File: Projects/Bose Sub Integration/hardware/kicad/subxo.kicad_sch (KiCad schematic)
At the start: 39 parts, among them J1 IN L, J2 IN R, J3 OUT 3.5mm, J4 PWR IN 15V, J5 POLARITY SW, J6 LEVEL POT 10k, U1 TL074, U2 LM7812

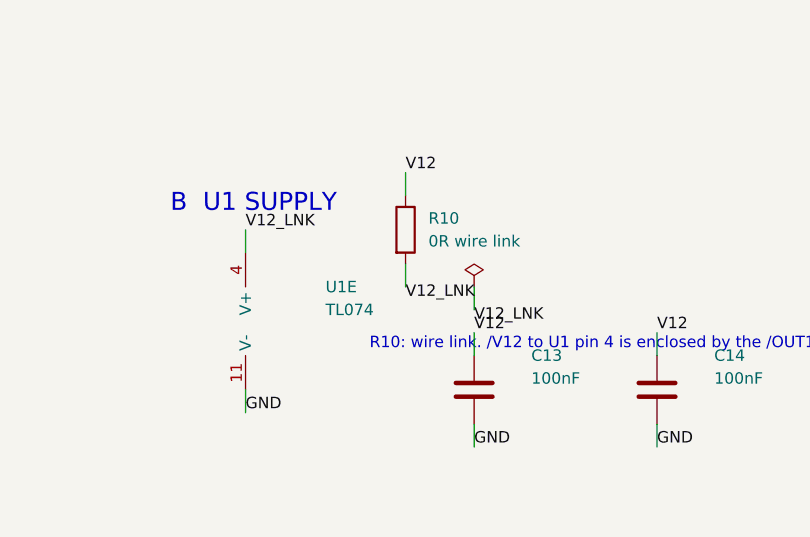
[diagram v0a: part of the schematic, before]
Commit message: Sub crossover board: re-placed, and the wire link is gone
The board committed in 28a28b6 only closed single-sided with R10, a 0 ohm
link flying over the tracks that sealed off U1 pin 4. Re-placing the parts
dissolves that pocket: /V12 now reaches pin 4 in copper. R10, the /V12_LNK
net it needed and the PWR_FLAG that marked that net as driven are all gone
from both the schematic and the layout.

185 track segments, every one on B.Cu, no vias and no top copper. DRC
reports 0 unconnected pads. The 15 violations that remain are silkscreen
only -- 12 overlaps and 3 clipped by mask -- and silkscreen is not in the
etched artwork, so none of them reach the board.

Outline comes down from 120.05 x 100.05 mm to 96.90 x 100.20 mm.

Zone rules now match the process instead of the KiCad defaults: minimum
clearance 0.5 -> 0.85 mm, and pads connect solid rather than through
thermal spokes.

Production files re-exported for the single-sided flow: B.Cu and Edge_Cuts
only, plus PTH drills, 100 holes across 0.8 / 1.0 / 1.1 / 1.2 / 1.52 mm.
The old two-sided set is dropped -- F.Cu, both solder masks, silkscreen and
the fab layer were never going to be made. The NPTH file exports empty.
Schematic is migrated to the KiCad 10 file format and stamped rev A.
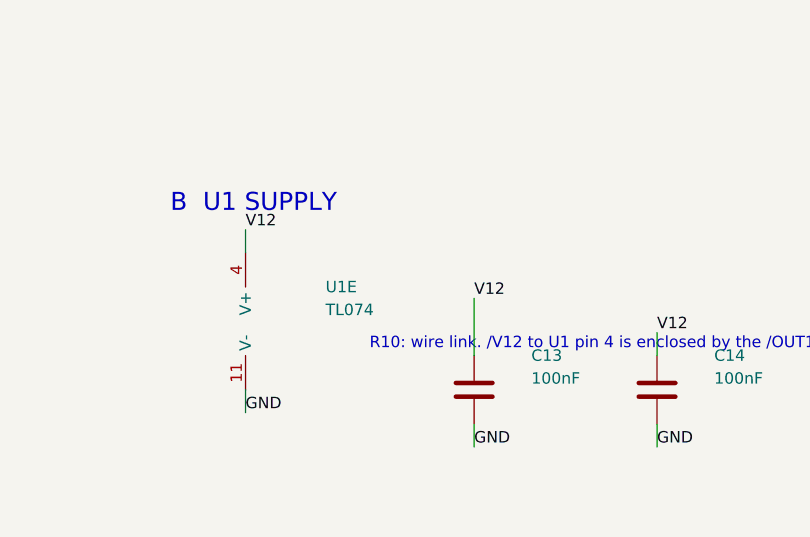
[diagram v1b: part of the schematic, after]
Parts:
- removed R10: 0R wire link, energy_system:WireLink_P14.50mm, symbol Device:R
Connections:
- net V12_LNK is gone; now on net V12: U1.4 (V+)

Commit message: Sub crossover: rev B schematic for the rotary switch and status LEDs
The wiring plan in the bring-up handoff was wrong. It had one header pin
feeding two switch lugs to get the C1_2 || C1_3 parallel setting, on the
argument that the rotary only ever connects the common to one position. But
splitting a wire to two lugs ties those lugs together permanently -- the switch
isolates common from lugs, not lugs from each other. A1 would have joined both
cap wires, shorting A2 to A3 through it, and all three positions would have
measured the same 365 nF.

So C1_1 is fitted at last, at 470 nF, and the parallel trick is retired. Every
lug now gets one distinct connection, and position 1 lands at 94.0 Hz -- the
first time the board reaches below 100 Hz, which is what the design wanted from
the start. The three ganged settings are 94.0 / 135.5 / 189.2 Hz, steps of 0.53
and 0.48 octave.

Capacitor values are now the as-built ones rather than the drawn ones: C2_2 is
the 120 nF that was actually soldered, not 100 nF. Every measured corner in the
results log depends on these, so the schematic may as well agree with the
hardware.

C_in gets a dual-pitch footprint, 5.00 mm and 15.00 mm on the same pads. Which
value is right is still a listening question -- 220 nF costs passband level but
damps the peaking, and Gate 11 has not run -- so the board takes either without
splaying leads across a footprint three times too wide. Same-number pads share
a net, so the extra pair costs nothing in mill clearance; the tightest
pad-1-to-pad-2 channel is 3.0 mm.

Two status LEDs. D1 is a power lamp on V12, which proves the regulator rather
than just the input. D2 rides SW2's second pole -- the polarity switch was
always a 2-pole changeover with one pole unused -- and lights only in the
inverted position, which matters because polarity is the largest audible
variable when integrating by ear. Both draw about 2 mA and neither touches a
signal node.

ERC 0 errors, and verify_netlist passes 115 checks inc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
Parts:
- added D1: PWR green, LED_THT:LED_D3.0mm, symbol Device:LED
- added D2: INV amber, LED_THT:LED_D3.0mm, symbol Device:LED
- added J7: INV LED, TerminalBlock:TerminalBlock_bornier-2_P5.08mm, symbol Connector:Screw_Terminal_01x02
- added R10, R11: 4k7, Resistor_THT:R_Axial_DIN0207_L6.3mm_D2.5mm_P7.62mm_Horizontal, symbol Device:R
- C1_1: value 330nF film -> 470nF film; footprint Capacitor_THT:C_Rect_L10.3mm_W5.7mm_P7.50mm_MKS4 -> Capacitor_THT:C_Rect_L13.0mm_W6.0mm_P10.00mm_FKS3_FKP3_MKS4
- C2_2: value 100nF film -> 120nF film
- C_in1, C_in2: value 2.2uF film -> 220n or 2u2; footprint Capacitor_THT:C_Rect_L18.0mm_W9.0mm_P15.00mm_FKS3_FKP3 -> energy_system:C_Rect_L18.0mm_W9.0mm_P5.00mm_P15.00mm_MultiPitch
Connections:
- net GND: now also D1.1 (K), J7.2 (Pin_2)
- net V12: now also R10.1, R11.1
- new net INV_A: D2.2 (A), R11.2
- new net INV_K: D2.1 (K), J7.1 (Pin_1)
- new net PWR_A: D1.2 (A), R10.2
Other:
- note added: "C1 returns to N1 -- the Sallen-Key feedback path. Not N2. JP1 selects C1 (odd pin = cap, even pin = N1); JP2 selects C2 (odd = cap, even = VGND). They select INDEPENDENTLY -- nine corners, not three pairs. Corners below are MEASURED on the rev A board, not calculated: the quoted f0 = 1/(2*pi*R*sqrt(C1*C2)) is not a -3 dB point, and C_in sits inside the filter. See Results - Sub Crossover Bring-up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"
- note added: "C_in1/C_in2 use a dual-pitch footprint: 5.00 mm for the 220n as built (or a 2u2 non-polarised electrolytic), 15.00 mm for a real 2u2 film part. Fit ONE pair. 220n puts ~8.8k of reactance in series with R1 at 82 Hz, so it is part of the filter, not just an input high-pass -- it costs 1.3-3.1 dB of passband level and damps the peaking. Whether that is a defect or a feature is a listening question; 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"
- note added: "D1 = power lamp on V12 (proves the LM7812, not just VIN). D2 = INVERTED lamp, fed from SW2's unused second pole via J7. Both ~2 mA. No LED touches a signal node."
- note added: "I STATUS LEDS"
- note removed: "C1 returns to N1 -- the Sallen-Key feedback path. Not N2. JP1/JP2 set the corner. ONE shunt in each, BOTH in the same position: 1-2 = 87 Hz (330n/150n) 3-4 = 130 Hz (220n/100n) 5-6 = 191 Hz (150n/68n) A mismatched pair gives the wrong Q, not an obvious fault."
- note removed: "R10: wire link. /V12 to U1 pin 4 is enclosed by the /OUT1 track and cannot be routed on one copper layer at any track width."

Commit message: Sub crossover: footprints from the measured parts, not from the values
Caliper readings on the real capacitors, inside-to-inside and
outside-to-outside. Those average to the pitch and differ by the lead diameter,
which came out at a consistent 0.5 mm on every part measured.

Three were wrong. C1_3 is a 10 mm part that rev A had on a 7.50 mm footprint,
which is why its leads had to be bent inward to fit. C2_2 is also 10 mm, body
12 x 4 mm, so the C2 bank is no longer three identical footprints in a row --
worth knowing before placing it. C1_1 came back at 5 mm rather than the 10 mm a
470n usually wants, so the generous 7.2 x 7.2 envelope of the P5.00 family goes
in until its body is measured.

C_in gains a third pitch at 10.00 mm alongside 5.00 and 15.00, because the part
earmarked for it measures about 10.5 mm. Pads sharing a number share a net, so
the extra pair needs no isolation from its own siblings and the tightest
pad-1-to-pad-2 channel is unchanged at 3.0 mm. The board can now take whichever
of the three the listening test ends up wanting.

ERC 0 errors, verify_netlist 115 of 115.
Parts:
- C1_1: footprint Capacitor_THT:C_Rect_L13.0mm_W6.0mm_P10.00mm_FKS3_FKP3_MKS4 -> Capacitor_THT:C_Rect_L7.2mm_W7.2mm_P5.00mm_FKS2_FKP2_MKS2_MKP2
- C1_3: footprint Capacitor_THT:C_Rect_L10.3mm_W5.7mm_P7.50mm_MKS4 -> Capacitor_THT:C_Rect_L13.0mm_W6.0mm_P10.00mm_FKS3_FKP3_MKS4
- C2_2: footprint Capacitor_THT:C_Rect_L7.2mm_W5.5mm_P5.00mm_FKS2_FKP2_MKS2_MKP2 -> Capacitor_THT:C_Rect_L13.0mm_W4.0mm_P10.00mm_FKS3_FKP3_MKS4
- C_in1, C_in2: footprint energy_system:C_Rect_L18.0mm_W9.0mm_P5.00mm_P15.00mm_MultiPitch -> energy_system:C_Rect_L18.0mm_W9.0mm_P5.00mm_P10.00mm_P15.00mm_MultiPitch
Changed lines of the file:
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@@
 			)
 		)
-		(property "Footprint" "energy_system:C_Rect_L18.0mm_W9.0mm_P5.00mm_P15.00mm_MultiPitch"
+		(property "Footprint" "energy_system:C_Rect_L18.0mm_W9.0mm_P5.00mm_P10.00mm_P15.00mm_MultiPitch"
 			(at 83.82 160.02 0)
 			(effects
@@
 			)
 		)
-		(property "Footprint" "energy_system:C_Rect_L18.0mm_W9.0mm_P5.00mm_P15.00mm_MultiPitch"
+		(property "Footprint" "energy_system:C_Rect_L18.0mm_W9.0mm_P5.00mm_P10.00mm_P15.00mm_MultiPitch"
 			(at 83.82 236.22 0)
 			(effects
@@
 			)
 		)
-		(property "Footprint" "Capacitor_THT:C_Rect_L13.0mm_W6.0mm_P10.00mm_FKS3_FKP3_MKS4"
+		(property "Footprint" "Capacitor_THT:C_Rect_L7.2mm_W7.2mm_P5.00mm_FKS2_FKP2_MKS2_MKP2"
 			(at 215.9 157.48 0)
 			(effects
@@
 			)
 		)
-		(property "Footprint" "Capacitor_THT:C_Rect_L10.3mm_W5.7mm_P7.50mm_MKS4"
+		(property "Footprint" "Capacitor_THT:C_Rect_L13.0mm_W6.0mm_P10.00mm_FKS3_FKP3_MKS4"
 			(at 215.9 182.88 0)
 			(effects
@@
 			)
 		)
-		(property "Footprint" "Capacitor_THT:C_Rect_L7.2mm_W5.5mm_P5.00mm_FKS2_FKP2_MKS2_MKP2"
+		(property "Footprint" "Capacitor_THT:C_Rect_L13.0mm_W4.0mm_P10.00mm_FKS3_FKP3_MKS4"
 			(at 215.9 256.54 0)
 			(effects

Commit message: Sub crossover: C1_2 is a 10 mm part too, and C_in stays at 220 nF
C1_2 measures 10.5 mm between leads, not the 5 mm the as-built BOM recorded.
That means its leads were squeezed inward to reach rev A's 7.50 mm footprint
rather than splayed outward as the note claimed, and it explains the rest of
the bending. It shares a footprint with C1_3 now, both on P10.00mm.

C_in1/C_in2 take the same 220 nF part, so the tri-pitch footprint's 10 mm
position is the one that gets populated and the measured response stands
unchanged at 94.0 / 135.5 / 189.2 Hz. The 5 mm and 15 mm pairs stay for the
2u2 option: fitting one would move the corners to 88 / 127 / 192 Hz and cut the
level spread between switch positions from 3.3 dB to 1.7 dB, which matters more
than the corner shift because loudness confounds an A/B comparison. That is
still a listening decision and Gate 11 has not run.

Pitches added to the BOM notes for the three parts re-measured today.

ERC 0 errors, verify_netlist 115 of 115.
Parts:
- C1_2: footprint Capacitor_THT:C_Rect_L10.3mm_W5.7mm_P7.50mm_MKS4 -> Capacitor_THT:C_Rect_L13.0mm_W6.0mm_P10.00mm_FKS3_FKP3_MKS4
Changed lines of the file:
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@@
 			)
 		)
-		(property "Footprint" "Capacitor_THT:C_Rect_L10.3mm_W5.7mm_P7.50mm_MKS4"
+		(property "Footprint" "Capacitor_THT:C_Rect_L13.0mm_W6.0mm_P10.00mm_FKS3_FKP3_MKS4"
 			(at 215.9 170.18 0)
 			(effects

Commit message: Sub crossover: real bodies on the C1 bank, and a footprint for the big 220n
Bodies measured, and no two C1 capacitors are the same part. C1_1 is 7.5 x 3.0
on a 5 mm pitch, C1_3 is 10.0 x 4.0 on 10 mm, and C1_2 is 16.0 x 7.0 on 10 mm.

C1_2 is the awkward one. A 16 mm body on a 10 mm pitch overhangs each lead by
3.0 mm, and the longest P10.00mm footprint in the stock library is L13.5 -- so
any stock choice under-reserves 3 mm at both ends and the part fouls whatever
is placed next to it. That is the same failure that left rev A with bent leads,
so it gets a measured footprint of its own in the project library instead. It
is now the largest part in the filter block and should be placed first.

C1_1 goes on L7.2 rather than the one true L7.5 part in the library, which is
3.5 mm wider than this cap needs. The 0.3 mm shortfall puts 0.15 mm of body
over each end of the silk, which is not worth a custom footprint.

The 18 x 9 envelope on the C_in multi-pitch footprint already clears the same
220n part at 16 x 7, so nothing changes there.

ERC 0 errors, verify_netlist 115 of 115.
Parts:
- C1_1: footprint Capacitor_THT:C_Rect_L7.2mm_W7.2mm_P5.00mm_FKS2_FKP2_MKS2_MKP2 -> Capacitor_THT:C_Rect_L7.2mm_W3.0mm_P5.00mm_FKS2_FKP2_MKS2_MKP2
- C1_2: footprint Capacitor_THT:C_Rect_L13.0mm_W6.0mm_P10.00mm_FKS3_FKP3_MKS4 -> energy_system:C_Rect_L16.0mm_W7.0mm_P10.00mm
- C1_3: footprint Capacitor_THT:C_Rect_L13.0mm_W6.0mm_P10.00mm_FKS3_FKP3_MKS4 -> Capacitor_THT:C_Rect_L11.0mm_W4.2mm_P10.00mm_MKT
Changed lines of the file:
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@@
 			)
 		)
-		(property "Footprint" "Capacitor_THT:C_Rect_L7.2mm_W7.2mm_P5.00mm_FKS2_FKP2_MKS2_MKP2"
+		(property "Footprint" "Capacitor_THT:C_Rect_L7.2mm_W3.0mm_P5.00mm_FKS2_FKP2_MKS2_MKP2"
 			(at 215.9 157.48 0)
 			(effects
@@
 			)
 		)
-		(property "Footprint" "Capacitor_THT:C_Rect_L13.0mm_W6.0mm_P10.00mm_FKS3_FKP3_MKS4"
+		(property "Footprint" "energy_system:C_Rect_L16.0mm_W7.0mm_P10.00mm"
 			(at 215.9 170.18 0)
 			(effects
@@
 			)
 		)
-		(property "Footprint" "Capacitor_THT:C_Rect_L13.0mm_W6.0mm_P10.00mm_FKS3_FKP3_MKS4"
+		(property "Footprint" "Capacitor_THT:C_Rect_L11.0mm_W4.2mm_P10.00mm_MKT"
 			(at 215.9 182.88 0)
 			(effects

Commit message: Sub crossover: C1_2 is a 15 mm part, and that settles C_in too
Re-measured properly: 14 mm inside the leads with 1 mm leads is a 15.00 mm
pitch, not the 10.5 mm the first reading suggested. That first pair implied a
0.1 mm lead, which was the tell that something was off.

So C1_2 goes on a stock P15.00mm footprint and the custom P10.00mm one written
an hour ago is deleted. L18 rather than the tighter L16.5, because L16.5 drills
1.1 mm and that is 0.1 mm of slack on a 1 mm lead; L18 drills 1.2, already in
the board's drill set. Two extra millimetres of reserved length is worth it on
a board that has already been fought into place once.

The knock-on is that C_in takes the same part, so it is a 15 mm part too and
rev A's bare 15.00 mm footprint was correct all along -- the BOM's "splayed
leads" note was simply wrong, and the leads were in fact squeezed in by 7.5 mm
to reach the 7.50 mm footprint at C1_2. The C_in multi-pitch footprint drops
back to 5.00 and 15.00; the 10.00 mm pair now serves no part and is removed.
5.00 stays for a 2u2 non-polarised electrolytic.

ERC 0 errors, verify_netlist 115 of 115.
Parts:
- C1_2: footprint energy_system:C_Rect_L16.0mm_W7.0mm_P10.00mm -> Capacitor_THT:C_Rect_L18.0mm_W7.0mm_P15.00mm_FKS3_FKP3
- C_in1, C_in2: footprint energy_system:C_Rect_L18.0mm_W9.0mm_P5.00mm_P10.00mm_P15.00mm_MultiPitch -> energy_system:C_Rect_L18.0mm_W9.0mm_P5.00mm_P15.00mm_MultiPitch
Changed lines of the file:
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@@
 			)
 		)
-		(property "Footprint" "energy_system:C_Rect_L18.0mm_W9.0mm_P5.00mm_P10.00mm_P15.00mm_MultiPitch"
+		(property "Footprint" "energy_system:C_Rect_L18.0mm_W9.0mm_P5.00mm_P15.00mm_MultiPitch"
 			(at 83.82 160.02 0)
 			(effects
@@
 			)
 		)
-		(property "Footprint" "energy_system:C_Rect_L18.0mm_W9.0mm_P5.00mm_P10.00mm_P15.00mm_MultiPitch"
+		(property "Footprint" "energy_system:C_Rect_L18.0mm_W9.0mm_P5.00mm_P15.00mm_MultiPitch"
 			(at 83.82 236.22 0)
 			(effects
@@
 			)
 		)
-		(property "Footprint" "energy_system:C_Rect_L16.0mm_W7.0mm_P10.00mm"
+		(property "Footprint" "Capacitor_THT:C_Rect_L18.0mm_W7.0mm_P15.00mm_FKS3_FKP3"
 			(at 215.9 170.18 0)
 			(effects
